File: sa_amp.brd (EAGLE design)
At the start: 80 x 80 mm, 87 parts, among them U4 TPA3255

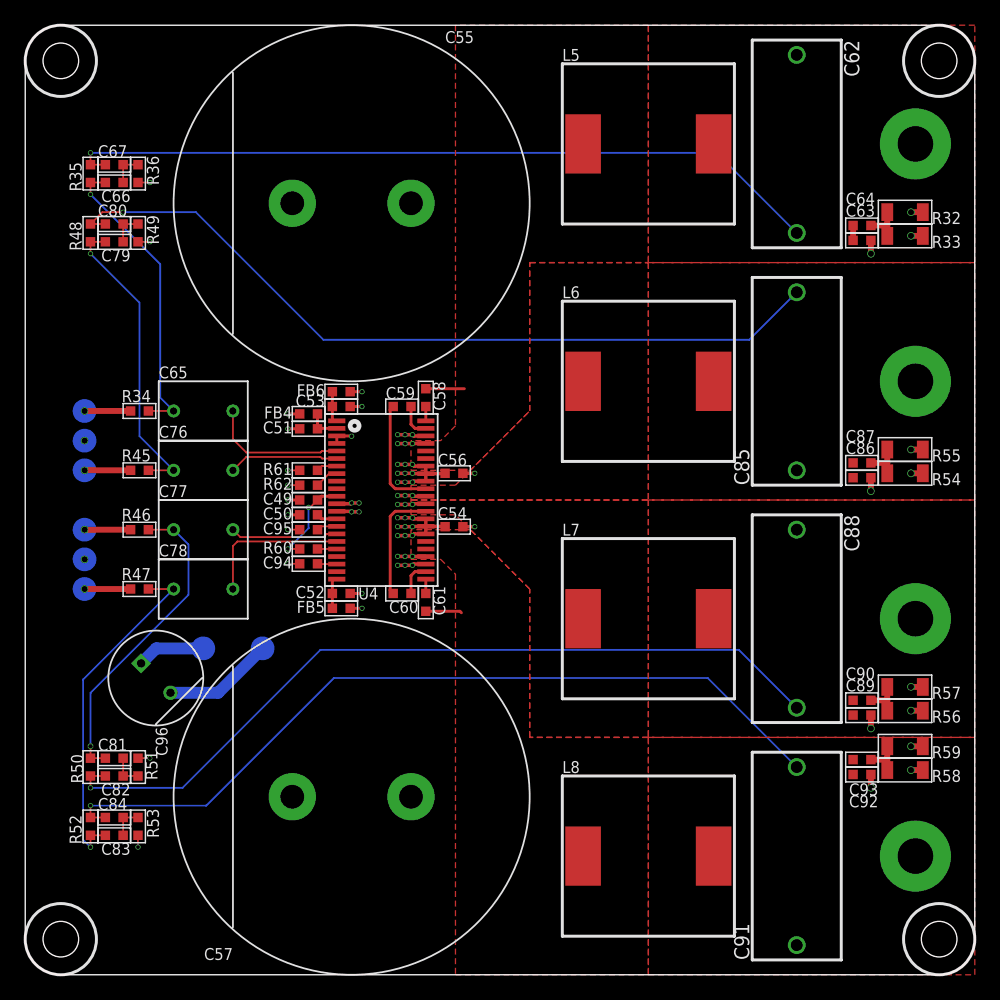
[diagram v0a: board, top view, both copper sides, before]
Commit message: Amplifier modules ready to be made
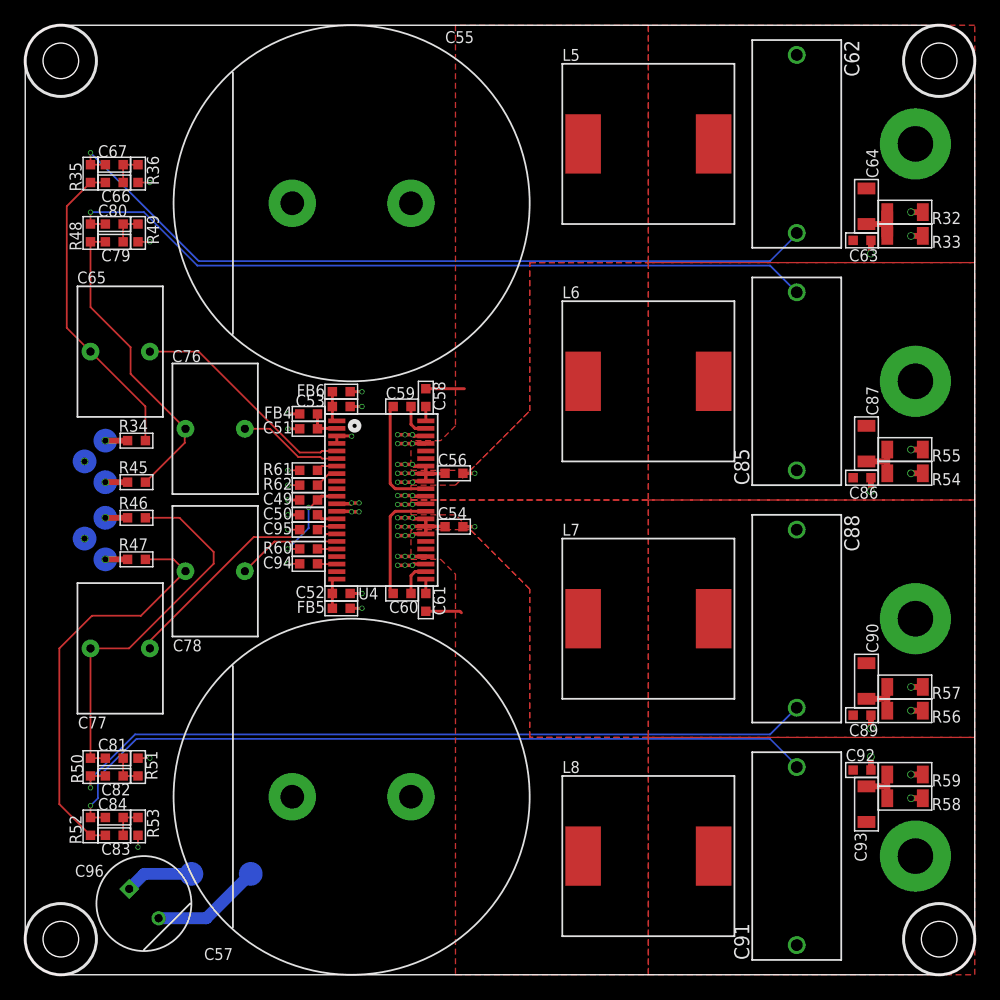
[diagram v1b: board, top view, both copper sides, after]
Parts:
- C64, C87, C90, C93: value 220nF 50V -> 220nF 100V; device CAPACITORS:0603 -> CAPACITORS:1206
- C65, C76, C77, C78: value 2.2uF 50V -> 10uF 50V; device CAPACITORS:5X7.2BOX -> CAPACITORS:7.2X11BOX
- C95: value 56nF 16V -> 47nF 16V
- moved C96 19.0 mm to (-20.0, -34.0)
- moved TP1 19.0 mm to (-16.0, -31.5)
- moved TP2 19.0 mm to (-11.0, -31.5)
- moved C77 12.2 mm to (-22.0, -12.5)
- moved C65 8.60 mm to (-22.0, 12.5)
- moved C93 3.77 mm to (40.9, -25.6), turned to 90 degrees
- moved C76 3.64 mm to (-14.0, 6.00)
- moved TP3 3.05 mm to (-23.2, 5.00)
- moved TP8 3.05 mm to (-23.2, -5.00)
- moved R34 2.51 mm to (-20.6, 5.00)
- moved R47 2.51 mm to (-20.6, -5.00)
- moved R58 2.38 mm to (44.1, -25.1)
- moved R59 2.38 mm to (44.1, -23.1)
- moved TP5 2.02 mm to (-23.2, 1.50)
- moved TP6 2.02 mm to (-23.2, -1.50)
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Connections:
- net TPA_VDD_1 renamed TPA_VDD
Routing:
- net 12V: track 53.6 -> 69.8 mm
- net N$76: track 9.12 -> 20.1 mm
- net N$61: track 11.6 -> 19.3 mm
- net N$81: track 29.5 -> 35.2 mm, vias 1 -> 0
- net N$2: track 26.6 -> 31.8 mm, vias 1 -> 0
- net N$77: track 12.5 -> 8.79 mm
- net N$82: track 68.6 -> 65.0 mm
- net N$85: track 69.3 -> 66.2 mm
- net N$79: track 67.3 -> 64.5 mm
- net N$6: track 3.88 -> 1.88 mm
- net N$5: track 3.88 -> 1.88 mm
- net N$4: track 3.88 -> 1.88 mm
- net N$3: track 3.88 -> 1.88 mm
- net N$60: track 3.38 -> 4.62 mm
- net N$62: track 25.5 -> 26.6 mm, vias 1 -> 0
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
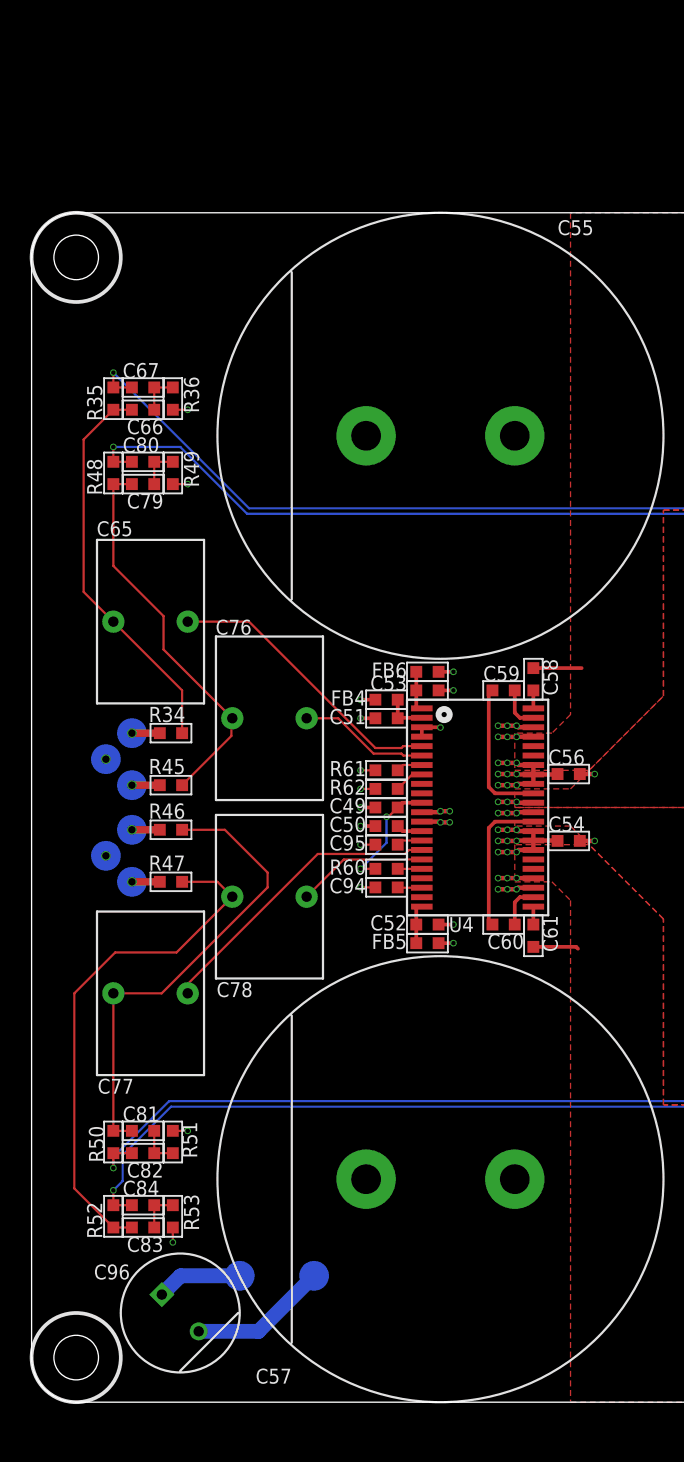
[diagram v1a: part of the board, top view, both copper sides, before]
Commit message: Master reset circuitry added
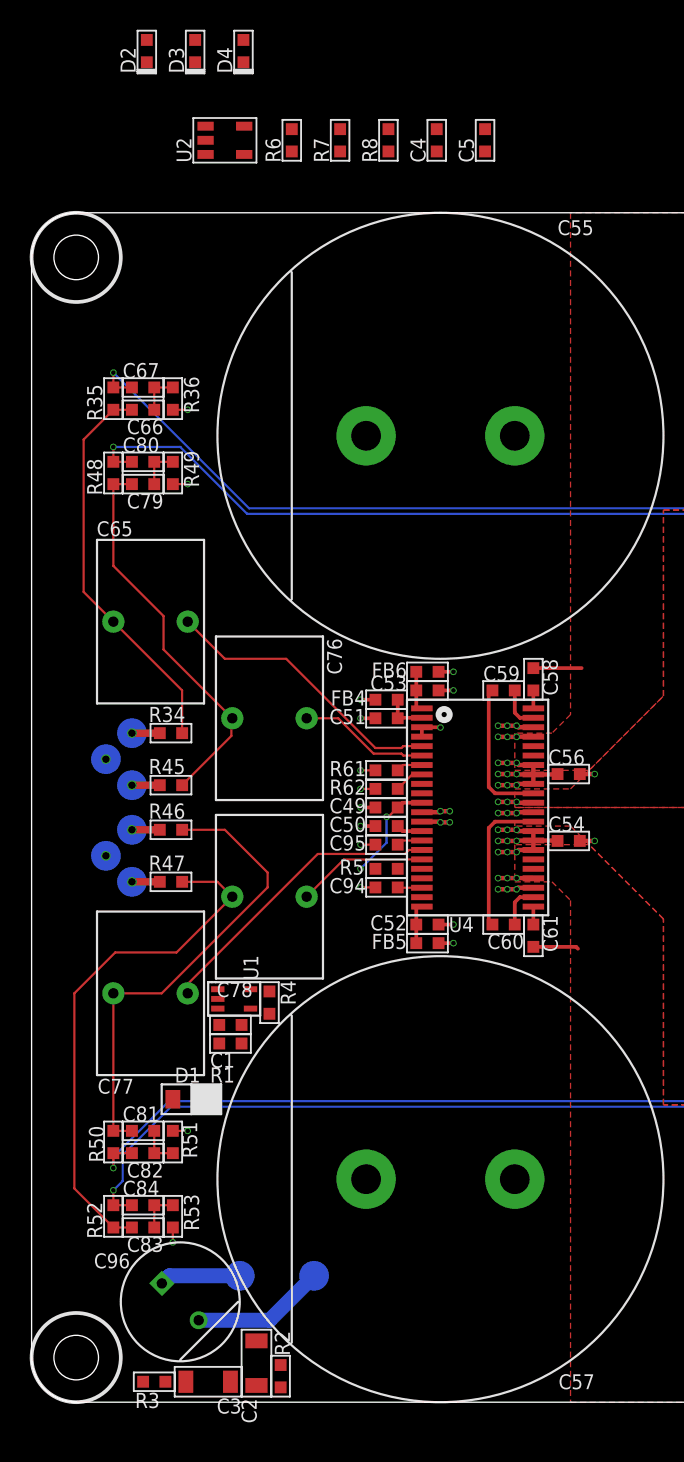
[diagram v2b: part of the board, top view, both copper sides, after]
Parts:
- added C1: 100nF 16V, CAPACITORS:0603
- added C2, C3: 1uF 50V, CAPACITORS:1206
- added C4, C5: 1uF 25V, CAPACITORS:0603
- added D1: 3V3, DIODES:SOD-323
- added D2, D3, D4: RED LED, OPTO:0603_POLAR
- added R1: 3.3k, r_0603:0603
- added R2: 6.8k, r_0603:0603
- added R3: 100k, r_0603:0603
- added R4: NO FIT, r_0603:0603
- added R6, R7, R8: 2.2k, r_0603:0603
- added U1: 2.93V Supervisor, ICs:SC70-5
- added U2: TPS70933, ICs:SOT23-5
- moved C96 0.75 mm to (-20.0, -33.2)
- renumbered R60 to R5
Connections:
- removed net N$90: R5.2, U4.18
- removed net TPA_VDD: C49.1, R5.1, U4.11
- new net !CLIP: D4.K, U4.21
- new net !FAULT: D3.K, U4.19
- new net !RESET: D2.K, R5.2, U1.3, U4.18
- new net 3V3: C49.1, U4.11
- new net N$10: D2.A, R6.1
- new net N$11: D3.A, R7.1
- new net N$12: D4.A, R8.1
- new net N$13: C5.2, R6.2, R7.2, R8.2, U2.5
- new net N$7: R4.1, U1.5
- new net N$8: C1.2, C2.2, C3.1, D1.K, R1.2, R2.1, R4.2, U1.4
- new net N$9: C3.2, R3.1
- net 12V: now also C4.2, R2.2, U2.1, U2.3
- net GND: now also C1.1, C2.1, C4.1, C5.1, D1.A, R1.1, R5.1, U1.1, U1.2, U2.2
- net VDD_AMP: now also R3.2
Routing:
- net TPA_VDD: track 7.99 -> 0.00 mm, vias 2 -> 0
- net 3V3: track 0.00 -> 6.99 mm, vias 0 -> 2
- net N$90: track 1.63 -> 0.00 mm
- net 12V: track 69.8 -> 68.8 mm

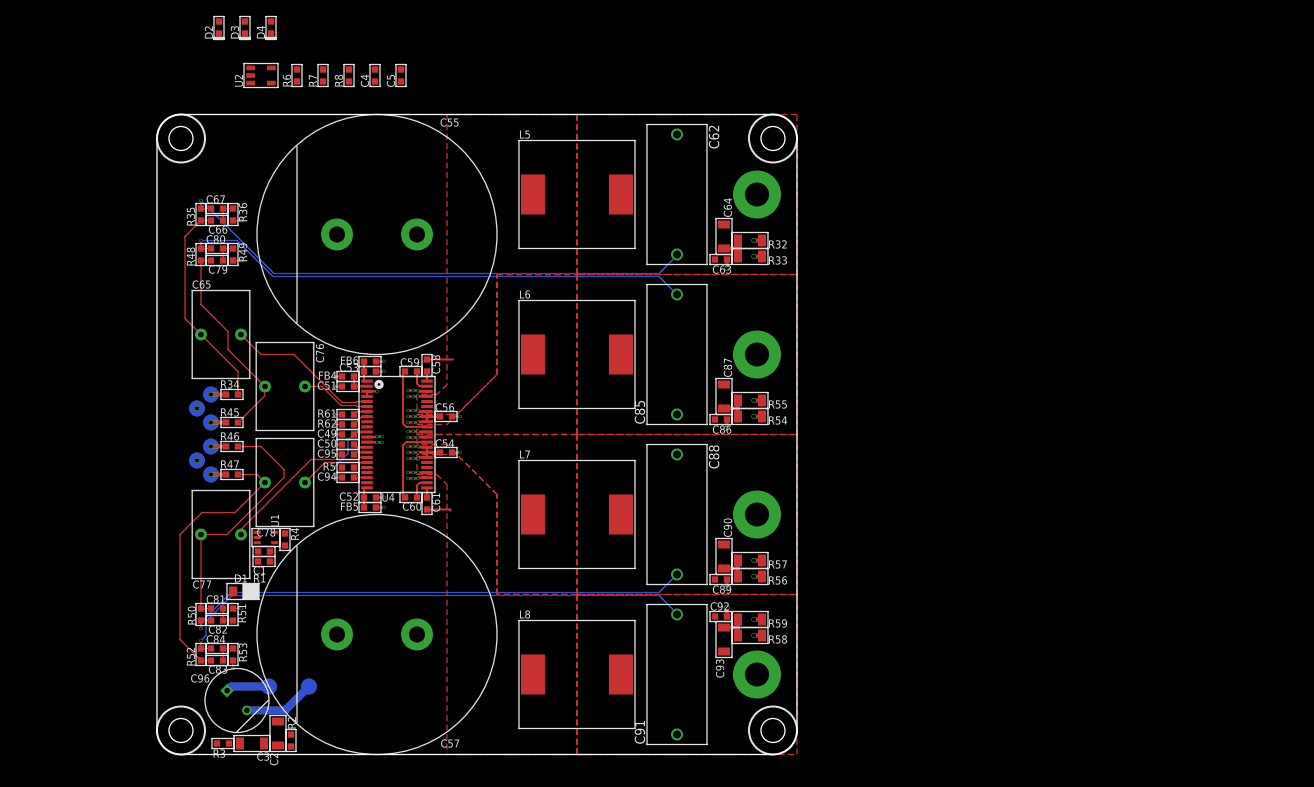
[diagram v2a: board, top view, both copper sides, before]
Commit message: New concept TPA3255 amplifier
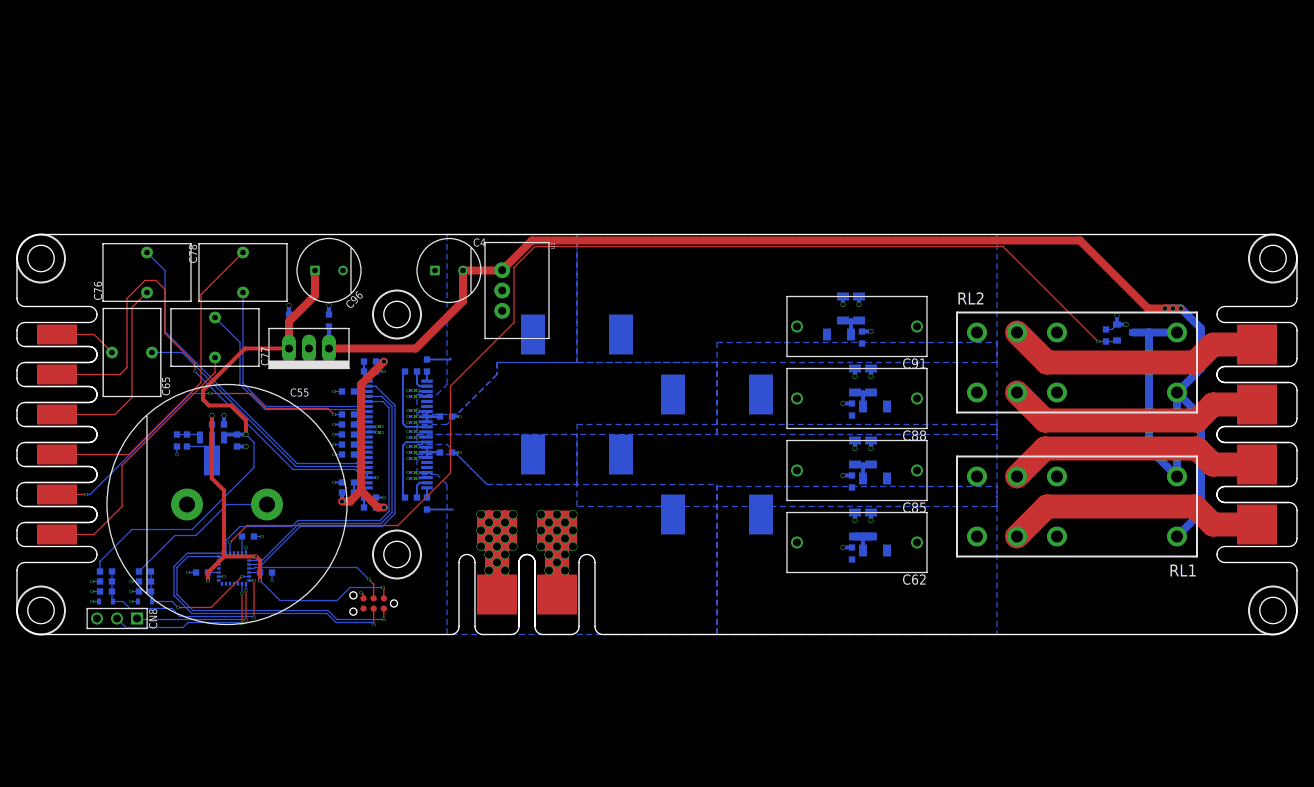
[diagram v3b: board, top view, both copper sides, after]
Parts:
- removed C57: 4700uF 63V, CAPACITORS:30MM_RADIAL_10MM_PITCH
- removed C66, C67, C79, C80, C81, C82, C83, C84: 220pF 50V, CAPACITORS:0603
- removed D4: RED LED, OPTO:0603_POLAR
- removed R34, R45, R46, R47: 2.7k, r_0603:0603
- removed R35, R48, R50, R52: 33k, r_0603:0603
- removed R36, R49, R51, R53: 10k, r_0603:0603
- removed TP1, TP2, TP3, TP4, TP5, TP6, TP7, TP8: 2MM_TEST_POINT, MISC:2MM_TEST_PAD
- added C6, C7, C9: 100nF 100V, CAPACITORS:0603
- added C8: 1uF 25V, CAPACITORS:0603
- added CN1, CN2, CN3, CN4, CN5, CN6: PCB Tab, CONNECTORs:PCB_TAB_SMALL
- added CN7: TC2030, tag-connect:TC2030-MCP
- added CN8: NO FIT, CONNECTORs:3PIN_HEADER
- added HOLE5, HOLE6: PCB Tab, CONNECTORs:PCB_TAB
- added MECH5, MECH6: 6mm x 3mm, MISC:MOUNTHOLE_6X3
- added Q1: 2N7002, TRANSISTORs:SOT23-3
- added RL1, RL2: RT424012, ELECTROMECH:30MMDPDTRELAY
- added U3: LM7812, ICs:TO220
- added U5: LM317, ICs:SOT89
- C1: value 100nF 16V -> 0.1uF 16V; device CAPACITORS:0603 -> c_0603:0603
- C2: value 1uF 50V -> 0.1uF 16V; device CAPACITORS:1206 -> c_0603:0603
- C3: value 1uF 50V -> 100nF 100V; device CAPACITORS:1206 -> CAPACITORS:0603
- C4: value 1uF 25V -> 100uF 50V; device CAPACITORS:0603 -> CAPACITORS:8MM_RADIAL_3.5MM_PITCH
- C5: value 1uF 25V -> 100nF 100V
- D1: value 3V3 -> PMEG4010BEA
- D2, D3: value RED LED -> PESD5Z3.3; device OPTO:0603_POLAR -> DIODES:SC-79
- HOLE1, HOLE2, HOLE3, HOLE4: value MOUNTHOLE_METAL6X3 -> PCB Tab; device MISC:MOUNTHOLE_6X3_METAL -> CONNECTORs:PCB_TAB
- R1: value 3.3k -> 47k
- R2: value 6.8k -> 47k
- R3: value 100k -> 240R
- R4: value NO FIT -> 390R
- R5: value 10k -> 1k
- R6: value 2.2k -> 18k
- R7: value 2.2k -> 10k
- R8: value 2.2k -> 36k
- U1: value 2.93V Supervisor -> STM32L031G6; device ICs:SC70-5 -> ICs:UFQPN28
- U2: value TPS70933 -> 15V REG; device ICs:SOT23-5 -> ICs:SRH05
- moved D1 118.4 mm to (97.5, 0.00), flipped to the bottom, turned to 90 degrees
- moved R1 109.0 mm to (88.6, 12.4), flipped to the bottom, turned to 270 degrees
- moved HOLE1 74.9 mm to (107.5, -11.2), turned to 270 degrees
- moved HOLE4 74.9 mm to (107.5, 11.2), turned to 270 degrees
- moved D3 73.8 mm to (-36.4, -20.9), flipped to the bottom
- moved D2 72.3 mm to (-31.5, -20.9), flipped to the bottom
- moved R8 69.0 mm to (-36.4, -17.1), flipped to the bottom, turned to 180 degrees
- moved R7 68.8 mm to (-36.4, -18.4), flipped to the bottom, turned to 180 degrees
- moved R6 64.8 mm to (-31.5, -17.1), flipped to the bottom, turned to 180 degrees
- moved MECH3 64.3 mm to (109.5, -22.0)
- moved MECH4 64.3 mm to (109.5, 22.0)
- moved HOLE2 64.0 mm to (107.5, -3.75), turned to 270 degrees
- moved HOLE3 64.0 mm to (107.5, 3.75), turned to 270 degrees
- moved C96 55.0 mm to (-8.50, 20.5), turned to 0 degrees
- moved C62 49.0 mm to (57.5, -13.5), turned to 180 degrees
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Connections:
- removed net !CLIP: D4.K, U4.21
- removed net !FAULT: D3.K, U4.19
- removed net !RESET: D2.K, R5.2, U1.3, U4.18
- removed net N$10: D2.A, R6.1
- removed net N$11: D3.A, R7.1
- removed net N$12: D4.A, R8.1
- removed net N$64: C66.2, C67.1, R36.1
- removed net N$7: R4.1, U1.5
- removed net N$78: C76.1, C79.1, R45.2, R48.1
- removed net N$80: C79.2, C80.1, R49.1
- removed net N$81: C78.1, C83.1, R47.2, R52.1
- removed net N$83: C81.2, C82.1, R51.1
- removed net N$85: C84.2, C91.2, C92.2, C93.2, HOLE4.P$1, L8.2, R52.2
- removed net N$86: C83.2, C84.1, R53.1
- new net 15V: C4.N, C5.1, D1.K, RL1.A1, RL2.A1, U2.3, U3.1
- new net N$14: C49.1, U4.11
- new net N$16: C78.1, CN6.1
- new net N$17: C76.1, CN3.1
- new net N$18: C77.1, CN4.1
- new net PROC_!RESET: CN7.3, U1.4
- new net PROC_SWCLK: CN7.4, U1.22
- new net PROC_SWDIO: CN7.2, U1.21
- new net PROC_UART_RX: CN8.2, U1.9
- new net PROC_UART_TX: CN8.1, U1.8
- new net PSU_12V_SENSE: C9.1, D3.K, R7.2, R8.2, U1.7
- new net PSU_VDD_AMP_SENSE: C3.1, D2.K, R5.2, R6.2, U1.6
- new net RLY_EN: Q1.1, R1.2, U1.24
- new net TPA_!CLIP: U1.3, U4.21
- new net TPA_!FAULT: U1.2, U4.19
- new net TPA_!RESET: U1.23, U4.18
- net 12V: now also C6.1, C7.1, R8.1, U3.3, U5.3; no longer C4.2, R2.2, TP1.1, U2.1, U2.3
- net 3V3: now also C1.2, C2.2, C8.2, CN7.1, R3.2, U1.1, U1.17, U1.5, U5.2; no longer C49.1, U4.11
- net GND: now also C3.2, C4.P, C5.2, C6.2, C7.2, C8.1, C9.2, CN2.1, CN5.1, CN7.5, CN8.3, D2.A, D3.A, HOLE6.1, Q1.3, R2.1, R4.1, R7.1, U1.16, U1.28, U3.2; no longer C4.1, C5.1, C57.1, D1.A, R36.2, R49.2, R51.2, R53.2, TP2.1, TP4.1, TP7.1, U1.1, U1.2
- net N$13: now also R3.1, R4.2, U5.1; no longer C5.2, R6.2, R7.2, R8.2, U2.5
- net N$2: now also C91.2, C92.2, C93.2, L8.2, RL2.24; no longer C77.1, C81.1, R46.2, R50.1
- net N$3: now also HOLE4.1, RL2.21; no longer R34.1, TP3.1
- net N$4: now also HOLE1.1, RL1.11; no longer R45.1, TP5.1
- net N$5: now also HOLE2.1, RL1.21; no longer R46.1, TP6.1
- net N$6: now also HOLE3.1, RL2.11; no longer R47.1, TP8.1
- net N$62: now also CN1.1; no longer C66.1, R34.2, R35.1
- net N$63: now also RL1.14; no longer C67.2, HOLE1.P$1, R35.2
- net N$79: now also RL1.24; no longer C80.2, HOLE2.P$1, R48.2
- net N$8: now also R2.2, U1.27; no longer C1.2, C2.2, C3.1, D1.K, R1.2, R2.1, R4.2, U1.4
- net N$82: now also RL2.14; no longer C82.2, HOLE3.P$1, R50.2
- net N$9: now also D1.A, Q1.2, RL1.A2, RL2.A2; no longer C3.2, R3.1
- net VDD_AMP: now also HOLE5.1, R6.1, U2.1; no longer C57.2, R3.2
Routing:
- net GND: track 56.6 -> 220.3 mm, vias 52 -> 86
- net 15V: track 0.00 -> 159.9 mm, vias 0 -> 3
- net RLY_EN: track 0.00 -> 142.9 mm, vias 0 -> 2
- net VDD_AMP: track 20.3 -> 119.0 mm, vias 18 -> 36
- net N$63: track 66.6 -> 0.00 mm, vias 1 -> 0
- net N$85: track 66.2 -> 0.00 mm, vias 1 -> 0
- net N$82: track 65.0 -> 0.00 mm, vias 1 -> 0
- net N$79: track 64.5 -> 0.00 mm, vias 1 -> 0
- net 3V3: track 6.99 -> 61.6 mm, vias 2 -> 5
- net 12V: track 68.8 -> 111.2 mm, vias 3 -> 4
- net N$16: track 0.00 -> 40.2 mm
- net TPA_!RESET: track 0.00 -> 39.5 mm
- net TPA_!CLIP: track 0.00 -> 38.9 mm
- net PROC_SWCLK: track 0.00 -> 38.8 mm, vias 0 -> 1
- net PROC_SWDIO: track 0.00 -> 37.7 mm, vias 0 -> 1
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- added copper zone on layer 3, net GND
- added copper zone on layer 16, net N$2
- added copper zone on layer 16, net N$53
- added copper zone on layer 16, net N$55
- added copper zone on layer 16, net N$57
- added copper zone on layer 16, net N$59
- added copper zone on layer 16, net N$63
- added copper zone on layer 16, net N$79
- added copper zone on layer 16, net N$82
- removed copper zone on layer 1, net N$53
- removed copper zone on layer 1, net N$55
- removed copper zone on layer 1, net N$57
- removed copper zone on layer 1, net N$59
- removed copper zone on layer 1, net N$63
- removed copper zone on layer 1, net N$79
- removed copper zone on layer 1, net N$82
- removed copper zone on layer 1, net N$85
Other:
- board size 80 x 80 mm -> 160 x 50 mm
